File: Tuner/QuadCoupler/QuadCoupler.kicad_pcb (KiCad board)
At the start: 2 copper layers, 100 x 100 mm, 109 parts, among them J1 Conn_01x01, J10 Conn_01x02, J11 Conn_01x01, J12 Conn_01x01, J13 Conn_01x01, J14 Conn_01x01, J15 Conn_01x01, J16 Conn_01x01, J17 Conn_01x01, J19 Conn_01x02, J2 Conn_Coaxial, J21 Conn_01x01, J22 Conn_01x01, J23 Conn_01x01, J24 Conn_01x01, J3 Conn_Coaxial, J4 Conn_Coaxial, J5 Conn_Coaxial, J6 Conn_Coaxial, J7 Conn_01x01, J8 Conn_01x01, J9 Conn_01x01

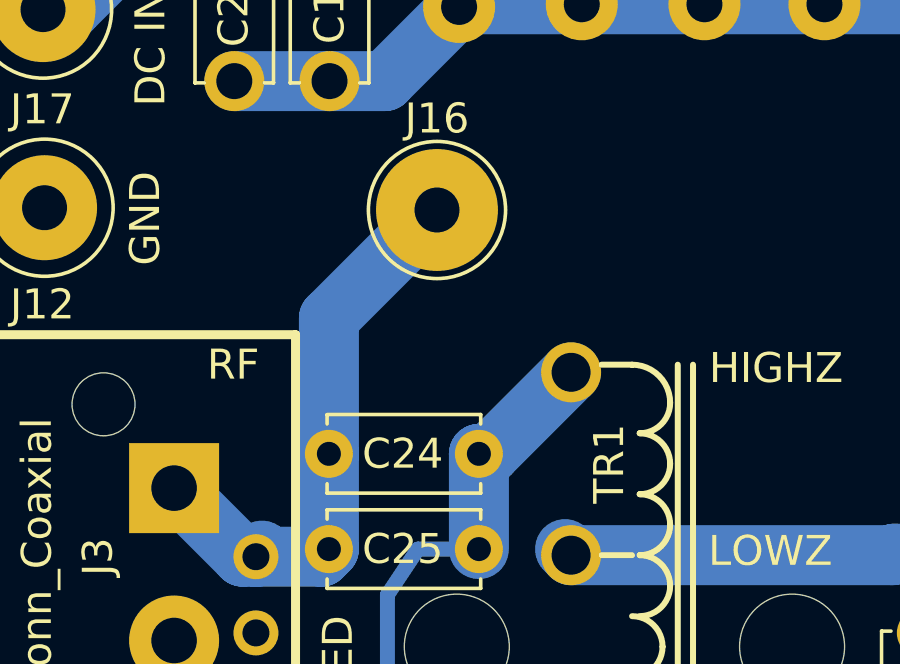
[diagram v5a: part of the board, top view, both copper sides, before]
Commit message: Added OptoisolatedRelay
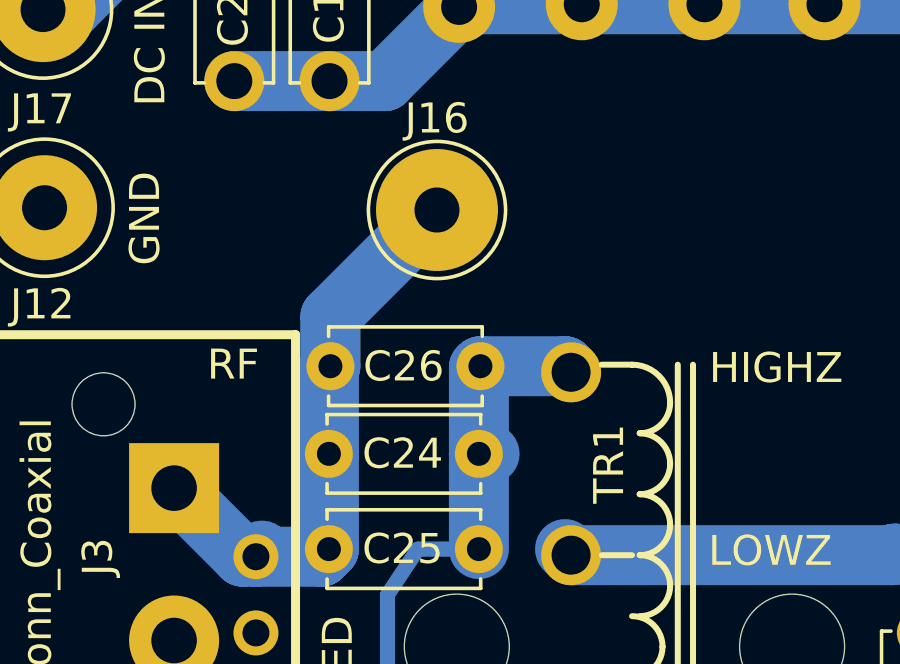
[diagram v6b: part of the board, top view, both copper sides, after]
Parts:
- added C26: NC, Capacitors_THT:C_Disc_D5.0mm_W2.5mm_P5.00mm, F.Cu at (59.7, 82.5)
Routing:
- net Net-(C24-Pad1): track 19.6 -> 21.8 mm
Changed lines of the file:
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@@
 (kicad_pcb (version 4) (host pcbnew 4.0.7)
   (general
-    (links 186)
+    (links 188)
     (no_connects 0)
     (area 39.924999 39.924999 140.075001 140.075001)
     (thickness 1.6)
     (drawings 58)
-    (tracks 347)
+    (tracks 352)
     (zones 0)
-    (modules 109)
+    (modules 110)
     (nets 34)
   )
@@
   )
   (setup
-    (last_trace_width 0.5)
+    (last_trace_width 2)
     (user_trace_width 0.35)
     (user_trace_width 0.5)
@@
       (net 33 "Net-(C24-Pad2)"))
   )
+  (module Capacitors_THT:C_Disc_D5.0mm_W2.5mm_P5.00mm (layer F.Cu)
+    (at 59.7408 82.55 180)
+    (descr "C, Disc series, Radial, pin pitch=5.00mm, , diameter*width=5*2.5mm^2, Capacitor, http://cdn-reichelt.de/documents/datenblatt/B300/DS_KERKO_TC.pdf")
+    (tags "C Disc series Radial pin pitch 5.00mm  diameter 5mm width 2.5mm Capacitor")
+    (fp_text reference C26 (at 2.5576 -0.011801 180) (layer F.SilkS)
+      (effects (font (size 1 1) (thickness 0.15)))
+    )
+    (fp_text value NC (at 2.5 2.56 180) (layer F.Fab)
+      (effects (font (size 1 1) (thickness 0.15)))
+    )
+    (fp_line (start 0 -1.25) (end 0 1.25) (layer F.Fab) (width 0.1))
+    (fp_line (start 0 1.25) (end 5 1.25) (layer F.Fab) (width 0.1))
+    (fp_line (start 5 1.25) (end 5 -1.25) (layer F.Fab) (width 0.1))
+    (fp_line (start 5 -1.25) (end 0 -1.25) (layer F.Fab) (width 0.1))
+    (fp_line (start -0.06 -1.31) (end 5.06 -1.31) (layer F.SilkS) (width 0.12))
+    (fp_line (start -0.06 1.31) (end 5.06 1.31) (layer F.SilkS) (width 0.12))
+    (fp_line (start -0.06 -1.31) (end -0.06 -0.996) (layer F.SilkS) (width 0.12))
+    (fp_line (start -0.06 0.996) (end -0.06 1.31) (layer F.SilkS) (width 0.12))
+    (fp_line (start 5.06 -1.31) (end 5.06 -0.996) (layer F.SilkS) (width 0.12))
+    (fp_line (start 5.06 0.996) (end 5.06 1.31) (layer F.SilkS) (width 0.12))
+    (fp_line (start -1.05 -1.6) (end -1.05 1.6) (layer F.CrtYd) (width 0.05))
+    (fp_line (start -1.05 1.6) (end 6.05 1.6) (layer F.CrtYd) (width 0.05))
+    (fp_line (start 6.05 1.6) (end 6.05 -1.6) (layer F.CrtYd) (width 0.05))
+    (fp_line (start 6.05 -1.6) (end -1.05 -1.6) (layer F.CrtYd) (width 0.05))
+    (fp_text user %R (at 2.5 0 180) (layer F.Fab)
+      (effects (font (size 1 1) (thickness 0.15)))
+    )
+    (pad 1 thru_hole circle (at 0 0 180) (size 1.6 1.6) (drill 0.8) (layers *.Cu *.Mask)
+      (net 32 "Net-(C24-Pad1)"))
+    (pad 2 thru_hole circle (at 5 0 180) (size 1.6 1.6) (drill 0.8) (layers *.Cu *.Mask)
+      (net 33 "Net-(C24-Pad2)"))
+    (model ${KISYS3DMOD}/Capacitors_THT.3dshapes/C_Disc_D5.0mm_W2.5mm_P5.00mm.wrl
+      (at (xyz 0 0 0))
+      (scale (xyz 1 1 1))
+      (rotate (xyz 0 0 0))
+    )
+  )
   (gr_text "RF CHOKES" (at 129.413 134.5692 90) (layer F.SilkS)
     (effects (font (size 1 1) (thickness 0.15)))
@@
   (segment (start 132.461 94.7547) (end 128.4605 94.7547) (width 2) (layer B.Cu) (net 18))
   (segment (start 83.693 94.869) (end 84.0994 94.869) (width 2) (layer B.Cu) (net 18) (status 30))
-  (segment (start 129.159 57.404) (end 130.7719 57.404) (width 0.5) (layer B.Cu) (net 19) (status 400000))
-  (segment (start 131.8768 74.041) (end 128.524 74.041) (width 0.5) (layer B.Cu) (net 19) (status 800000))
+  (segment (start 129.159 57.404) (end 130.7719 57.404) (width 0.5) (layer B.Cu) (net 19))
+  (segment (start 131.8768 74.041) (end 128.524 74.041) (width 0.5) (layer B.Cu) (net 19))
   (segment (start 135.2296 70.6882) (end 131.8768 74.041) (width 0.5) (layer B.Cu) (net 19))
   (segment (start 135.2296 61.8617) (end 135.2296 70.6882) (width 0.5) (layer B.Cu) (net 19))
@@
   (segment (start 62.5602 88.646) (end 62.7634 88.8492) (width 0.5) (layer B.Cu) (net 20))
   (segment (start 62.5602 88.646) (end 62.7634 88.8492) (width 2) (layer B.Cu) (net 20))
-  (segment (start 117.3988 63.1444) (end 117.1194 63.1444) (width 0.5) (layer B.Cu) (net 21) (status C00000))
-  (segment (start 117.1194 63.1444) (end 114.7953 65.4685) (width 0.5) (layer B.Cu) (net 21) (status 400000))
+  (segment (start 117.3988 63.1444) (end 117.1194 63.1444) (width 0.5) (layer B.Cu) (net 21))
+  (segment (start 117.1194 63.1444) (end 114.7953 65.4685) (width 0.5) (layer B.Cu) (net 21))
   (segment (start 104.394 63.9064) (end 105.2068 63.9064) (width 2) (layer B.Cu) (net 21))
   (segment (start 105.2068 63.9064) (end 105.4608 63.6524) (width 2) (layer B.Cu) (net 21))
@@
   (segment (start 139.319 58.2295) (end 137.16 56.0705) (width 1) (layer B.Cu) (net 31))
   (segment (start 137.16 56.0705) (end 134.6835 56.0705) (width 1) (layer B.Cu) (net 31))
+  (segment (start 59.7408 82.55) (end 62.5602 82.55) (width 2) (layer B.Cu) (net 32) (status C00000))
+  (segment (start 62.5602 82.55) (end 62.7634 82.7532) (width 2) (layer B.Cu) (net 32) (status C00000))
+  (segment (start 59.69 85.471) (end 59.69 82.6008) (width 2) (layer B.Cu) (net 32) (status C00000))
+  (segment (start 59.69 82.6008) (end 59.7408 82.55) (width 2) (layer B.Cu) (net 32) (status C00000))
   (segment (start 59.69 88.646) (end 57.658 88.646) (width 0.5) (layer B.Cu) (net 32))
   (segment (start 56.642 94.869) (end 58.8645 97.7265) (width 0.5) (layer B.Cu) (net 32))
@@
   (segment (start 57.658 88.646) (end 56.642 90.17) (width 0.5) (layer B.Cu) (net 32))
   (segment (start 59.69 85.471) (end 60.0456 85.471) (width 2) (layer B.Cu) (net 32))
-  (segment (start 60.0456 85.471) (end 62.7634 82.7532) (width 2) (layer B.Cu) (net 32))
   (segment (start 59.69 85.471) (end 59.69 88.646) (width 2) (layer B.Cu) (net 32))
+  (segment (start 54.7408 82.55) (end 54.7408 80.8952) (width 2) (layer B.Cu) (net 33) (status 400000))
+  (segment (start 54.7408 80.8952) (end 58.293 77.343) (width 2) (layer B.Cu) (net 33) (status 800000))
+  (segment (start 54.69 85.471) (end 54.69 82.6008) (width 2) (layer B.Cu) (net 33) (status C00000))
+  (segment (start 54.69 82.6008) (end 54.7408 82.55) (width 2) (layer B.Cu) (net 33) (status C00000))
   (segment (start 54.69 85.471) (end 54.69 88.646) (width 2) (layer B.Cu) (net 33))
-  (segment (start 54.69 85.471) (end 54.69 80.946) (width 2) (layer B.Cu) (net 33))
-  (segment (start 54.69 80.946) (end 58.293 77.343) (width 2) (layer B.Cu) (net 33))
   (segment (start 52.258 88.9) (end 54.436 88.9) (width 2) (layer B.Cu) (net 33))
   (segment (start 54.436 88.9) (end 54.69 88.646) (width 2) (layer B.Cu) (net 33))

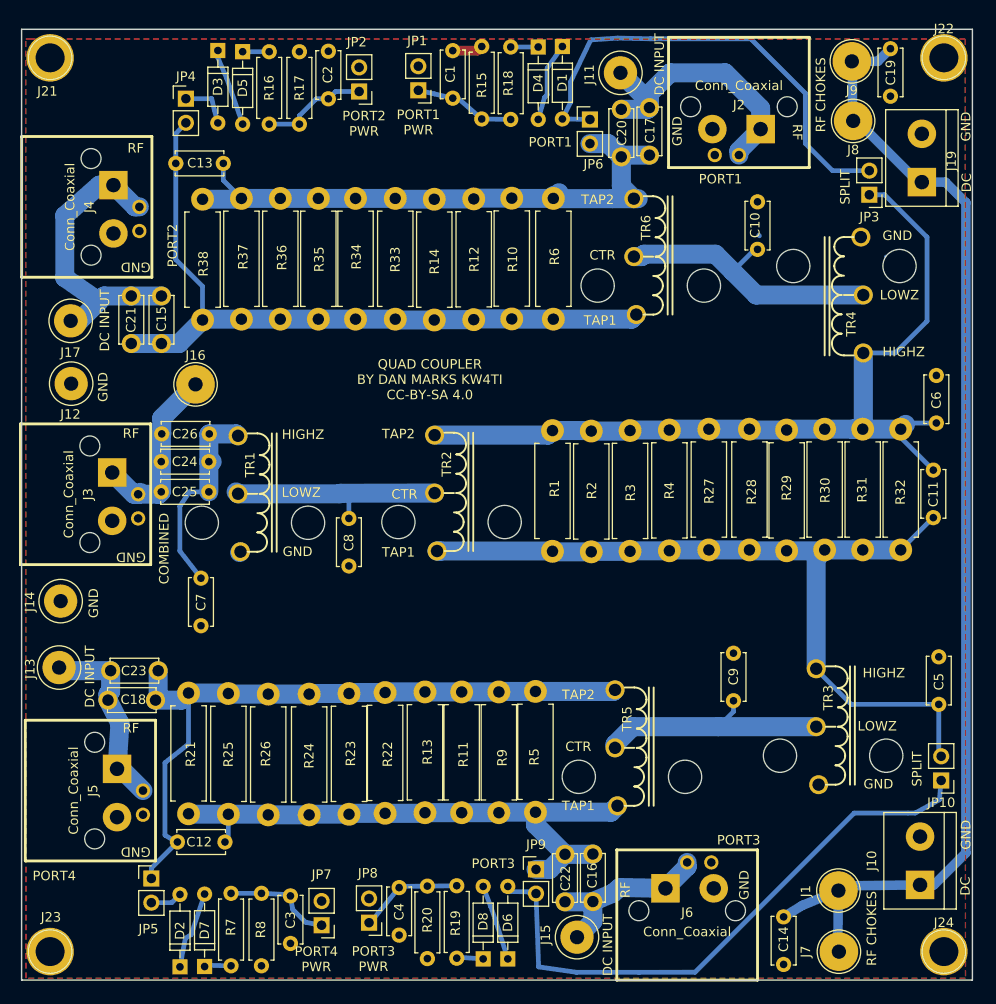
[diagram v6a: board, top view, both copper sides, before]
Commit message: Some modifications to Quadcoupler for easier access
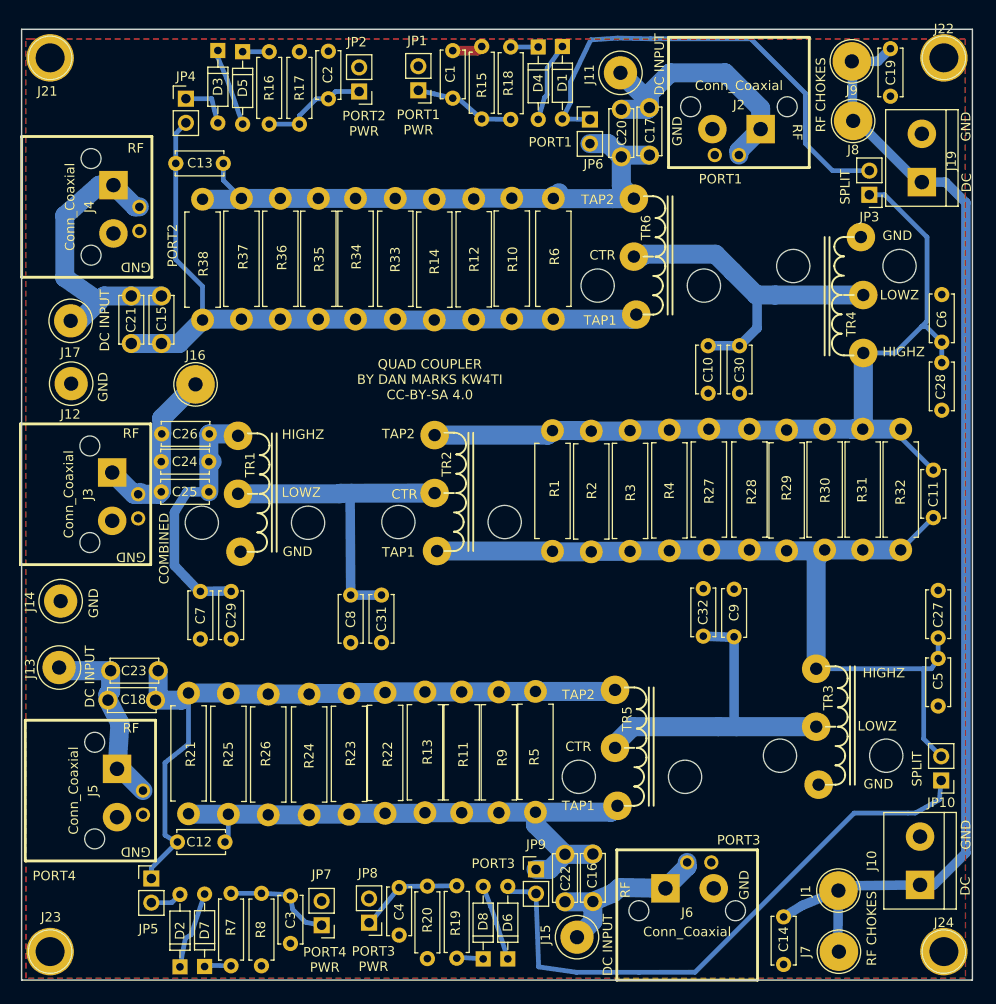
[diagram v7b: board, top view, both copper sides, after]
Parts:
- added C27: NC, Capacitors_THT:C_Disc_D5.0mm_W2.5mm_P5.00mm, F.Cu at (136.4, 104.0)
- added C28: NC, Capacitors_THT:C_Disc_D5.0mm_W2.5mm_P5.00mm, F.Cu at (136.8, 75.1)
- added C29: NC, Capacitors_THT:C_Disc_D5.0mm_W2.5mm_P5.00mm, F.Cu at (62.0, 99.1)
- added C30: 47 pF 1 kV, Capacitors_THT:C_Disc_D5.0mm_W2.5mm_P5.00mm, F.Cu at (115.5, 73.3)
- added C31: 68 pF 1 kV, Capacitors_THT:C_Disc_D5.0mm_W2.5mm_P5.00mm, F.Cu at (77.9, 99.5)
- added C32: 47 pF 1 kV, Capacitors_THT:C_Disc_D5.0mm_W2.5mm_P5.00mm, F.Cu at (111.7, 103.8)
- C10, C9: value NC -> 47 pF 1 kV
- C16, C17, C20, C22, C24, C25, C26: value NC -> 10 nF 1 kV
- C8: value NC -> 68 pF 1 kV
- moved C10 11.4 mm to (112.2, 73.3), turned to 270 degrees
- moved C6 8.53 mm to (136.8, 72.9)
- moved C8 8.07 mm to (74.6, 99.5)
- moved C9 6.73 mm to (114.9, 103.9)
- moved C5 4.83 mm to (136.4, 106.2), turned to 270 degrees
- moved C7 1.40 mm to (58.8, 99.1)
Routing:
- net Net-(C31-Pad1): track 24.3 -> 35.5 mm
- net Net-(C32-Pad1): track 25.7 -> 35.6 mm
- net Net-(C11-Pad2): track 87.3 -> 93.2 mm
- net Net-(C10-Pad1): track 29.6 -> 35.4 mm
- net Net-(C24-Pad1): track 21.8 -> 27.2 mm
- net (no net): track 2.12 -> 0.00 mm
- net Net-(C11-Pad1): track 96.1 -> 97.2 mm

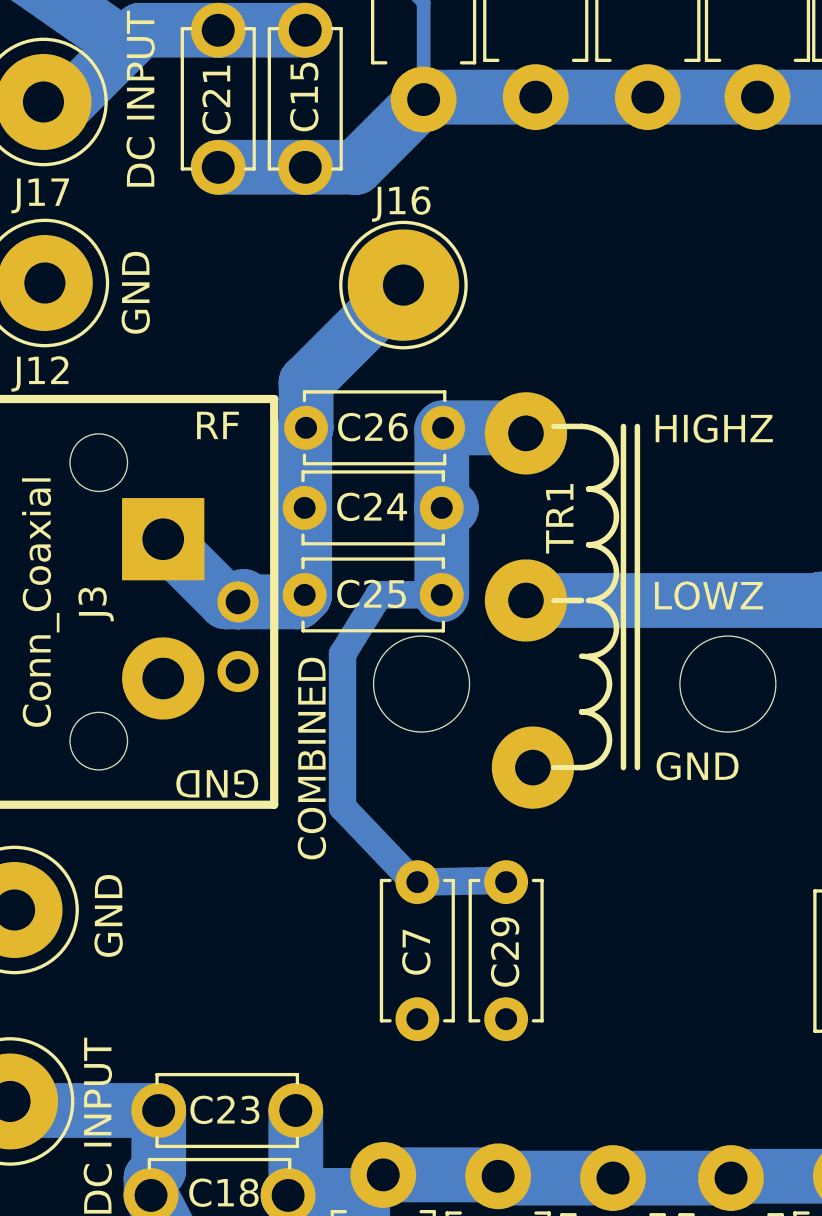
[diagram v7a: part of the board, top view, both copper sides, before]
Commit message: Added switchable low pass filter PCB
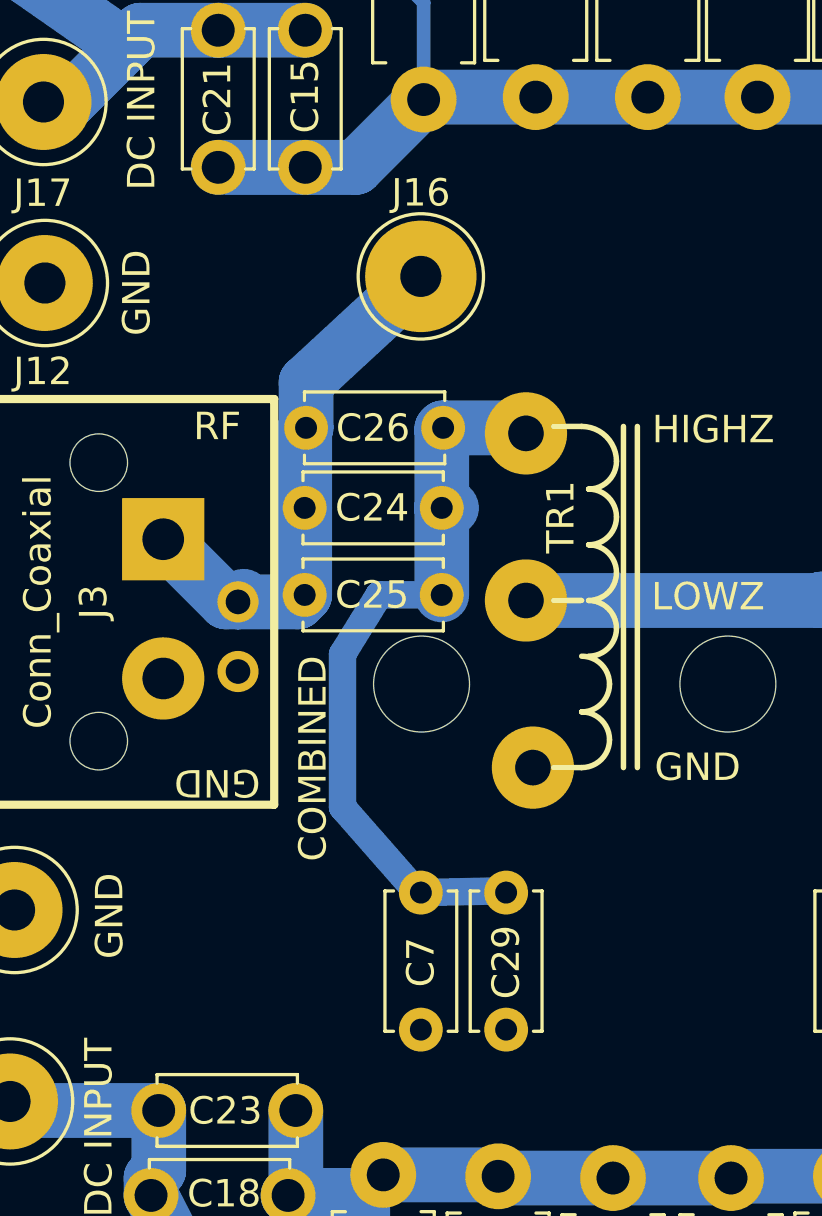
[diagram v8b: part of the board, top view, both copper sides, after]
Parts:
- moved J16 0.71 mm to (58.9, 77.0)
- moved C7 0.40 mm to (58.9, 99.5)
- moved C29 0.38 mm to (62.0, 99.5)
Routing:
- net Net-(C24-Pad2): track 19.3 -> 20.0 mm
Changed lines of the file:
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@@
   )
   (module Capacitors_THT:C_Disc_D5.0mm_W2.5mm_P5.00mm (layer F.Cu)
-    (at 58.801 99.1235 270)
+    (at 58.928 99.5045 270)
     (descr "C, Disc series, Radial, pin pitch=5.00mm, , diameter*width=5*2.5mm^2, Capacitor, http://cdn-reichelt.de/documents/datenblatt/B300/DS_KERKO_TC.pdf")
     (tags "C Disc series Radial pin pitch 5.00mm  diameter 5mm width 2.5mm Capacitor")
@@
   )
   (module Connectors:1pin (layer F.Cu)
-    (at 58.293 77.343)
+    (at 58.928 77.0255)
     (descr "module 1 pin (ou trou mecanique de percage)")
     (tags DEV)
@@
   )
   (module Capacitors_THT:C_Disc_D5.0mm_W2.5mm_P5.00mm (layer F.Cu)
-    (at 62.0395 99.1235 270)
+    (at 62.0395 99.5045 270)
     (descr "C, Disc series, Radial, pin pitch=5.00mm, , diameter*width=5*2.5mm^2, Capacitor, http://cdn-reichelt.de/documents/datenblatt/B300/DS_KERKO_TC.pdf")
     (tags "C Disc series Radial pin pitch 5.00mm  diameter 5mm width 2.5mm Capacitor")
@@
   (segment (start 137.16 56.0705) (end 134.6835 56.0705) (width 1) (layer B.Cu) (net 29))
   (segment (start 62.5602 82.55) (end 62.7634 82.7532) (width 2) (layer B.Cu) (net 30))
-  (segment (start 58.801 99.1235) (end 61.976 99.06) (width 1) (layer B.Cu) (net 30) (status 20))
-  (segment (start 61.976 99.06) (end 62.0395 99.1235) (width 1) (layer B.Cu) (net 30) (status 30))
+  (segment (start 58.928 99.5045) (end 61.976 99.441) (width 1) (layer B.Cu) (net 30) (status 10))
+  (segment (start 61.976 99.441) (end 62.0395 99.5045) (width 1) (layer B.Cu) (net 30) (status 30))
   (segment (start 59.69 88.646) (end 57.404 88.646) (width 1) (layer B.Cu) (net 30))
-  (segment (start 56.0705 96.393) (end 58.674 99.1235) (width 1) (layer B.Cu) (net 30) (status 20))
+  (segment (start 56.0705 96.393) (end 58.801 99.5045) (width 1) (layer B.Cu) (net 30) (status 20))
   (segment (start 56.0705 90.805) (end 56.0705 96.393) (width 1) (layer B.Cu) (net 30))
   (segment (start 57.404 88.646) (end 56.0705 90.805) (width 1) (layer B.Cu) (net 30))
-  (segment (start 58.674 99.1235) (end 58.801 99.1235) (width 1) (layer B.Cu) (net 30) (status 30))
-  (segment (start 61.976 99.06) (end 62.0395 99.1235) (width 0.5) (layer B.Cu) (net 30) (status 30))
+  (segment (start 58.801 99.5045) (end 58.928 99.5045) (width 1) (layer B.Cu) (net 30) (status 30))
+  (segment (start 61.976 99.441) (end 62.0395 99.5045) (width 0.5) (layer B.Cu) (net 30) (status 30))
   (segment (start 59.7408 82.55) (end 62.5602 82.55) (width 2) (layer B.Cu) (net 30))
   (segment (start 59.69 85.471) (end 59.69 82.6008) (width 2) (layer B.Cu) (net 30))
@@
   (segment (start 59.69 85.471) (end 59.69 88.646) (width 2) (layer B.Cu) (net 30))
   (segment (start 54.7408 82.55) (end 54.7408 80.8952) (width 2) (layer B.Cu) (net 31))
-  (segment (start 54.7408 80.8952) (end 58.293 77.343) (width 2) (layer B.Cu) (net 31))
+  (segment (start 54.7408 80.8952) (end 58.928 77.0255) (width 2) (layer B.Cu) (net 31) (status 20))
   (segment (start 54.69 85.471) (end 54.69 82.6008) (width 2) (layer B.Cu) (net 31))
   (segment (start 54.69 82.6008) (end 54.7408 82.55) (width 2) (layer B.Cu) (net 31))
